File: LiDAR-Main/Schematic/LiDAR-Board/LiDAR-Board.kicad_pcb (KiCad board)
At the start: 2 copper layers, 8 parts, among them Q1 NPN, Q2 NPN, U1 Pico

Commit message: PCB Finished w/earths
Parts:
- added J1: Conn_01x04, HEVCS_Sensor_Footprints:Conn_01x04_MOLEX, F.Cu at (49.3, 20.3)
- moved R1 45.8 mm to (76.2, 66.0)
- moved Q2 44.1 mm to (82.2, 67.6)
- moved R2 43.7 mm to (76.2, 68.6)
- moved Q1 43.6 mm to (82.2, 61.9)
- moved U4 37.8 mm to (40.6, 48.3)
- moved U1 28.1 mm to (59.8, 52.1)
- moved U2 28.1 mm to (104.1, 33.0)
- moved U3 28.1 mm to (104.1, 48.3)
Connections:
- net +5V renamed 5V_MAIN_BOARD
- R1 pad 1: Net-(U1-GPIO21) -> Net-(U1-GPIO19)
- R2 pad 1: Net-(U1-GPIO20) -> Net-(U1-GPIO18)
- U1 pad 17: unconnected-(U1-GPIO13-Pad17) -> IMU_INT
- U1 pad 18: IMU_INT -> unconnected-(U1-GND-Pad18)
- U1 pad 19: INT_1 -> unconnected-(U1-GPIO14-Pad19)
- U1 pad 20: INT_2 -> unconnected-(U1-GPIO15-Pad20)
- U1 pad 21: unconnected-(U1-GPIO16-Pad21) -> INT_2
- U1 pad 22: unconnected-(U1-GPIO17-Pad22) -> INT_1
- U1 pad 23: unconnected-(U1-GND-Pad23) -> Earth
- U1 pad 24: unconnected-(U1-GPIO18-Pad24) -> Net-(U1-GPIO18)
- U1 pad 25: unconnected-(U1-GPIO19-Pad25) -> Net-(U1-GPIO19)
- U1 pad 26: Net-(U1-GPIO20) -> SDA
- U1 pad 27: Net-(U1-GPIO21) -> SCL
- U1 pad 3: unconnected-(U1-GND-Pad3) -> Earth
- U1 pad 6: SCL -> unconnected-(U1-GPIO4-Pad6)
- U1 pad 7: SDA -> unconnected-(U1-GPIO5-Pad7)
- U2 pad 5: (no net) -> Earth
- U3 pad 5: (no net) -> Earth
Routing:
- net SDA: track 0.00 -> 146.1 mm
- net INT_1: track 0.00 -> 105.8 mm
- net 3V3_BOARD_OUT: track 0.00 -> 74.4 mm
- net INT_2: track 0.00 -> 61.5 mm
- net 5V_MAIN_BOARD: track 0.00 -> 57.8 mm
- net Earth: track 0.00 -> 54.5 mm
- net Net-(Q1-C): track 0.00 -> 40.4 mm
- net Net-(Q2-C): track 0.00 -> 33.5 mm
- net SCL: track 0.00 -> 28.8 mm
- net IMU_INT: track 0.00 -> 21.0 mm
- net UART_0_RX: track 0.00 -> 15.0 mm
- net IMU_SDA: track 0.00 -> 10.3 mm
- net IMU_SCL: track 0.00 -> 10.3 mm
- net UART_0_TX: track 0.00 -> 7.66 mm
- net Net-(U1-GPIO19): track 0.00 -> 6.69 mm
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
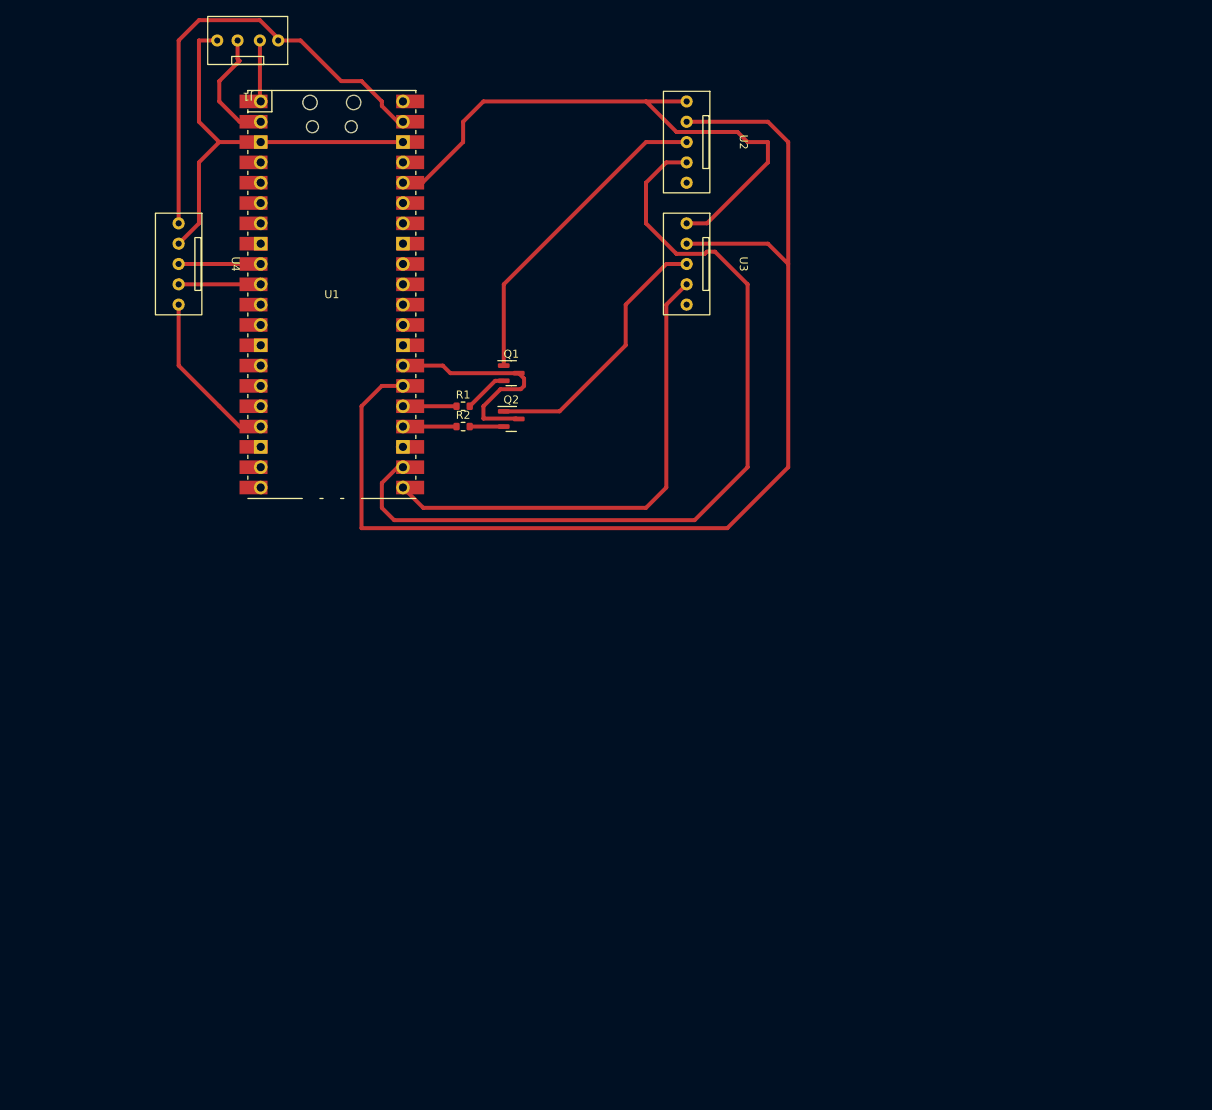
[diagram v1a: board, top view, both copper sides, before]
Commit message: Refactor PCB - can be reverted if wanted :)
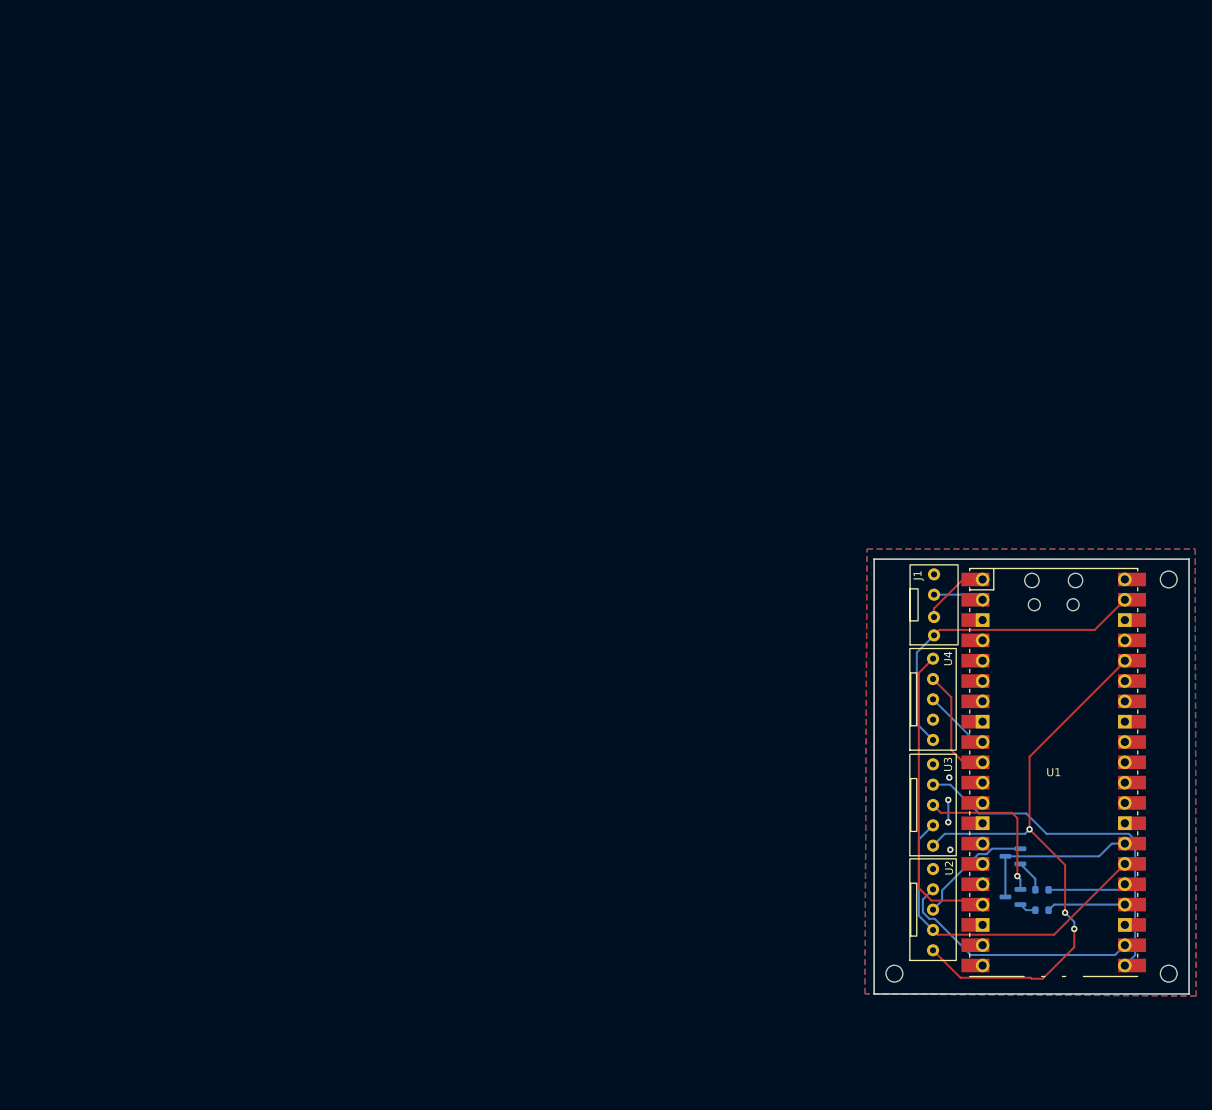
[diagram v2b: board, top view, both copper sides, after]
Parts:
- added REF**: MountingHole_2.1mm, MountingHole:MountingHole_2.1mm, F.Cu at (164.4, 137.0)
- added REF**: MountingHole_2.1mm, MountingHole:MountingHole_2.1mm, F.Cu at (130.1, 137.0)
- added REF**: MountingHole_2.1mm, MountingHole:MountingHole_2.1mm, F.Cu at (164.4, 87.7)
- Q1, Q2, R1, R2: moved to B.Cu
- moved J1 111.1 mm to (135.1, 90.9), turned to 90 degrees
- moved U4 108.9 mm to (134.9, 102.7), turned to 90 degrees
- moved U1 108.2 mm to (150.0, 111.8)
- moved U2 100.8 mm to (134.9, 129.0), turned to 90 degrees
- moved R2 94.3 mm to (148.6, 129.0), turned to 180 degrees
- moved R1 94.3 mm to (148.6, 126.5), turned to 180 degrees
- moved Q1 87.1 mm to (144.9, 122.3), turned to 180 degrees
- moved Q2 86.6 mm to (144.9, 127.4), turned to 180 degrees
- moved U3 74.3 mm to (134.9, 115.9), turned to 90 degrees
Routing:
- net SDA: track 146.1 -> 42.4 mm
- net INT_1: track 105.8 -> 31.4 mm
- net Earth: track 54.5 -> 2.79 mm, vias 0 -> 4
- net Net-(Q1-C): track 40.4 -> 14.8 mm
- net 5V_MAIN_BOARD: track 57.8 -> 40.5 mm
- net IMU_INT: track 21.0 -> 38.2 mm
- net INT_2: track 61.5 -> 44.4 mm
- net Net-(Q2-C): track 33.5 -> 20.3 mm, vias 0 -> 1
- net UART_0_RX: track 15.0 -> 6.33 mm
- net SCL: track 28.8 -> 20.7 mm
- net IMU_SDA: track 10.3 -> 14.4 mm
- net Net-(U1-GPIO18): track 6.69 -> 9.82 mm
- net Net-(U1-GPIO19): track 6.69 -> 9.82 mm
- net 3V3_BOARD_OUT: track 74.4 -> 76.7 mm, vias 0 -> 3
- net Net-(Q2-B): track 4.25 -> 2.16 mm
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- added copper zone on B.Cu, net Earth
- added copper zone on F.Cu, net Earth
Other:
- board outline added: 39.4 x 54.4 mm

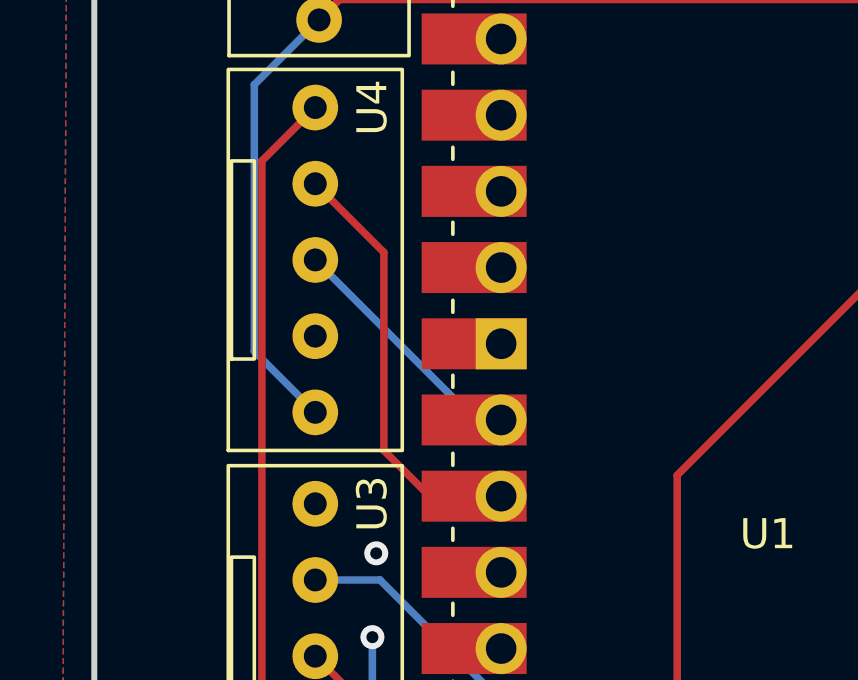
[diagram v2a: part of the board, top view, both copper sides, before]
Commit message: Fixed IMU I2C Pin allocation
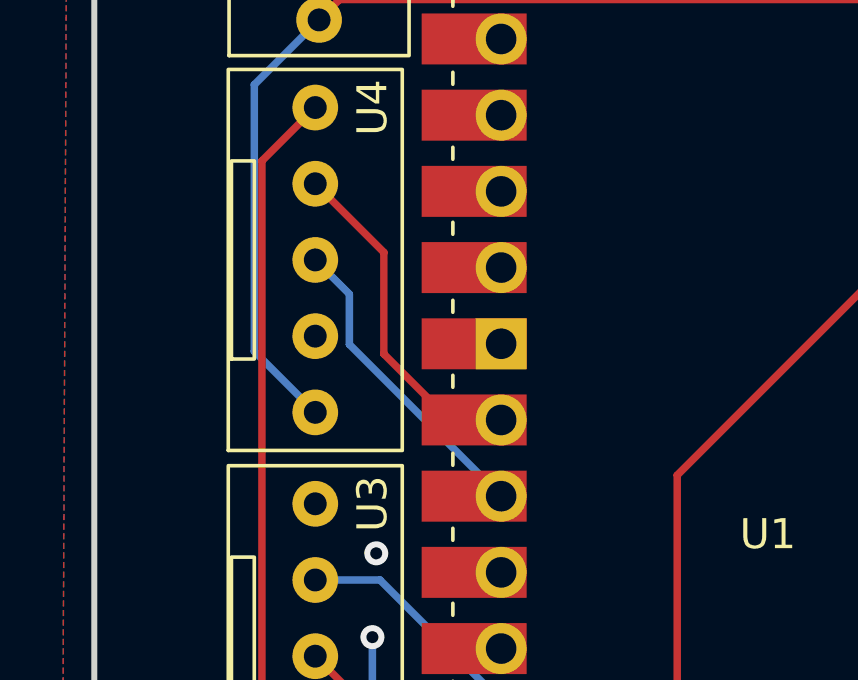
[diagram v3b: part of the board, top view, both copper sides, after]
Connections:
- U1 pad 10: IMU_SDA -> IMU_SCL
- U1 pad 9: IMU_SCL -> IMU_SDA
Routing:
- net IMU_SDA: track 14.4 -> 11.4 mm
- net IMU_SCL: track 8.41 -> 10.4 mm
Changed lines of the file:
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@@
       (net 11 "unconnected-(U1-GND-Pad8)") (pinfunction "GND") (pintype "power_in+no_connect"))
     (pad "9" thru_hole oval (at -8.89 -3.81) (size 1.7 1.7) (drill 1.02) (layers "*.Cu" "*.Mask")
-      (net 12 "IMU_SCL") (pinfunction "GPIO6") (pintype "bidirectional"))
+      (net 13 "IMU_SDA") (pinfunction "GPIO6") (pintype "bidirectional"))
     (pad "9" smd rect (at -8.89 -3.81) (size 3.5 1.7) (drill (offset -0.9 0)) (layers "F.Cu" "F.Mask")
-      (net 12 "IMU_SCL") (pinfunction "GPIO6") (pintype "bidirectional"))
+      (net 13 "IMU_SDA") (pinfunction "GPIO6") (pintype "bidirectional"))
     (pad "10" thru_hole oval (at -8.89 -1.27) (size 1.7 1.7) (drill 1.02) (layers "*.Cu" "*.Mask")
-      (net 13 "IMU_SDA") (pinfunction "GPIO7") (pintype "bidirectional"))
+      (net 12 "IMU_SCL") (pinfunction "GPIO7") (pintype "bidirectional"))
     (pad "10" smd rect (at -8.89 -1.27) (size 3.5 1.7) (drill (offset -0.9 0)) (layers "F.Cu" "F.Mask")
-      (net 13 "IMU_SDA") (pinfunction "GPIO7") (pintype "bidirectional"))
+      (net 12 "IMU_SCL") (pinfunction "GPIO7") (pintype "bidirectional"))
     (pad "11" thru_hole oval (at -8.89 1.27) (size 1.7 1.7) (drill 1.02) (layers "*.Cu" "*.Mask")
-      (net 14 "unconnected-(U1-GPIO8-Pad11)") (pinfunction "GPIO8") (pintype "bidirectional+no_connect"))
+      (net 14 "unconnected-(U1-GPIO8-Pad11)") (pinfunction "GPIO8") (pintype "bidirectional"))
     (pad "11" smd rect (at -8.89 1.27) (size 3.5 1.7) (drill (offset -0.9 0)) (layers "F.Cu" "F.Mask")
-      (net 14 "unconnected-(U1-GPIO8-Pad11)") (pinfunction "GPIO8") (pintype "bidirectional+no_connect"))
+      (net 14 "unconnected-(U1-GPIO8-Pad11)") (pinfunction "GPIO8") (pintype "bidirectional"))
     (pad "12" thru_hole oval (at -8.89 3.81) (size 1.7 1.7) (drill 1.02) (layers "*.Cu" "*.Mask")
       (net 15 "unconnected-(U1-GPIO9-Pad12)") (pinfunction "GPIO9") (pintype "bidirectional+no_connect"))
@@
   (segment (start 134.94 131.506) (end 133.17 129.736) (width 0.25) (layer "B.Cu") (net 10))
   (segment (start 133.17 129.736) (end 133.17 120.195) (width 0.25) (layer "B.Cu") (net 10))
-  (segment (start 134.94 102.677) (end 140.274 108.011) (width 0.25) (layer "B.Cu") (net 12))
-  (segment (start 140.274 108.011) (end 141.136 108.011) (width 0.25) (layer "B.Cu") (net 12))
-  (segment (start 138.75 110.551) (end 141.136 110.551) (width 0.25) (layer "F.Cu") (net 13))
-  (segment (start 137.226 109.027) (end 138.75 110.551) (width 0.25) (layer "F.Cu") (net 13))
-  (segment (start 134.94 100.137) (end 137.226 102.423) (width 0.25) (layer "F.Cu") (net 13))
-  (segment (start 137.226 102.423) (end 137.226 109.027) (width 0.25) (layer "F.Cu") (net 13))
+  (segment (start 136.077 105.492) (end 141.136 110.551) (width 0.25) (layer "B.Cu") (net 12))
+  (segment (start 134.94 102.677) (end 136.077 103.814) (width 0.25) (layer "B.Cu") (net 12))
+  (segment (start 136.077 103.814) (end 136.077 105.492) (width 0.25) (layer "B.Cu") (net 12))
+  (segment (start 137.226 102.423) (end 134.94 100.137) (width 0.25) (layer "F.Cu") (net 13))
+  (segment (start 137.226 105.811) (end 137.226 102.423) (width 0.25) (layer "F.Cu") (net 13))
+  (segment (start 141.136 108.011) (end 139.426 108.011) (width 0.25) (layer "F.Cu") (net 13))
+  (segment (start 139.426 108.011) (end 137.226 105.811) (width 0.25) (layer "F.Cu") (net 13))
   (segment (start 133.162 99.375) (end 133.162 126.255961) (width 0.25) (layer "F.Cu") (net 20))
   (segment (start 140.634 127.829) (end 141.136 128.331) (width 0.25) (layer "F.Cu") (net 20))

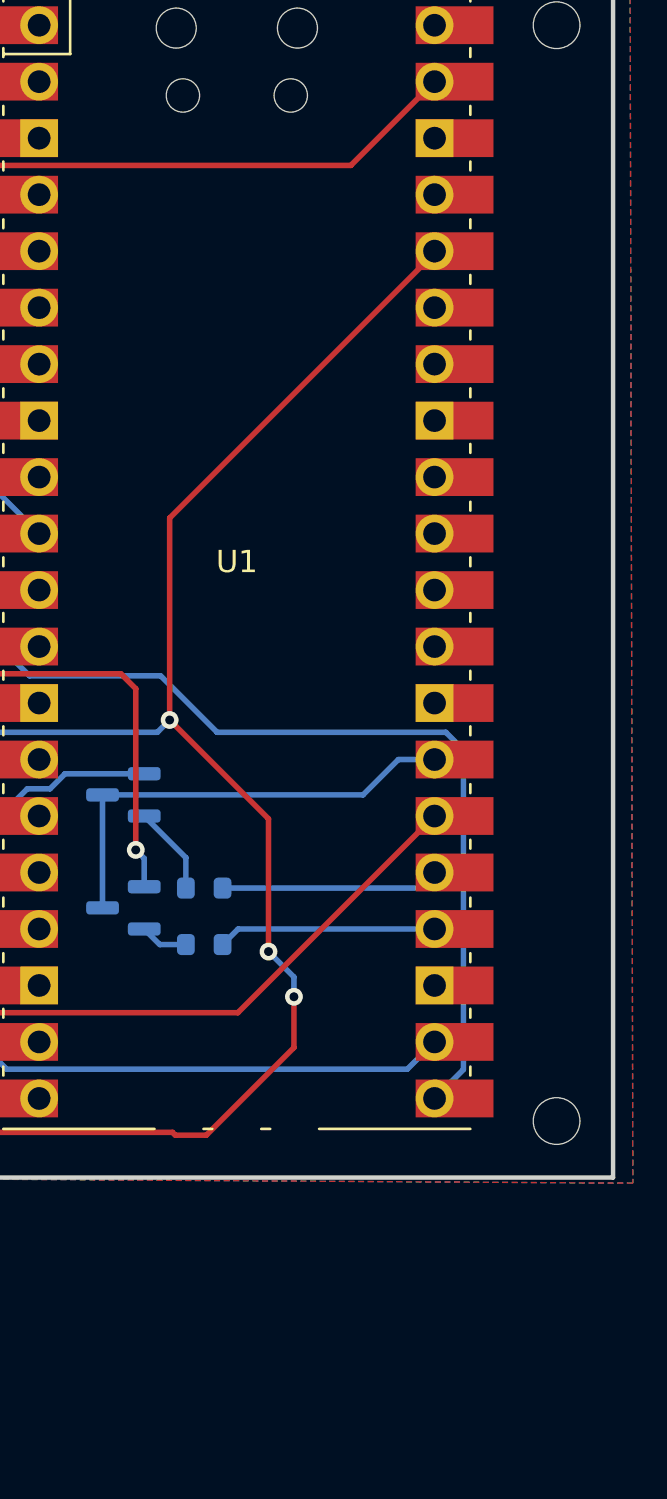
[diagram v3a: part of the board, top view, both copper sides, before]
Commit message: PCB Silkscreen changes
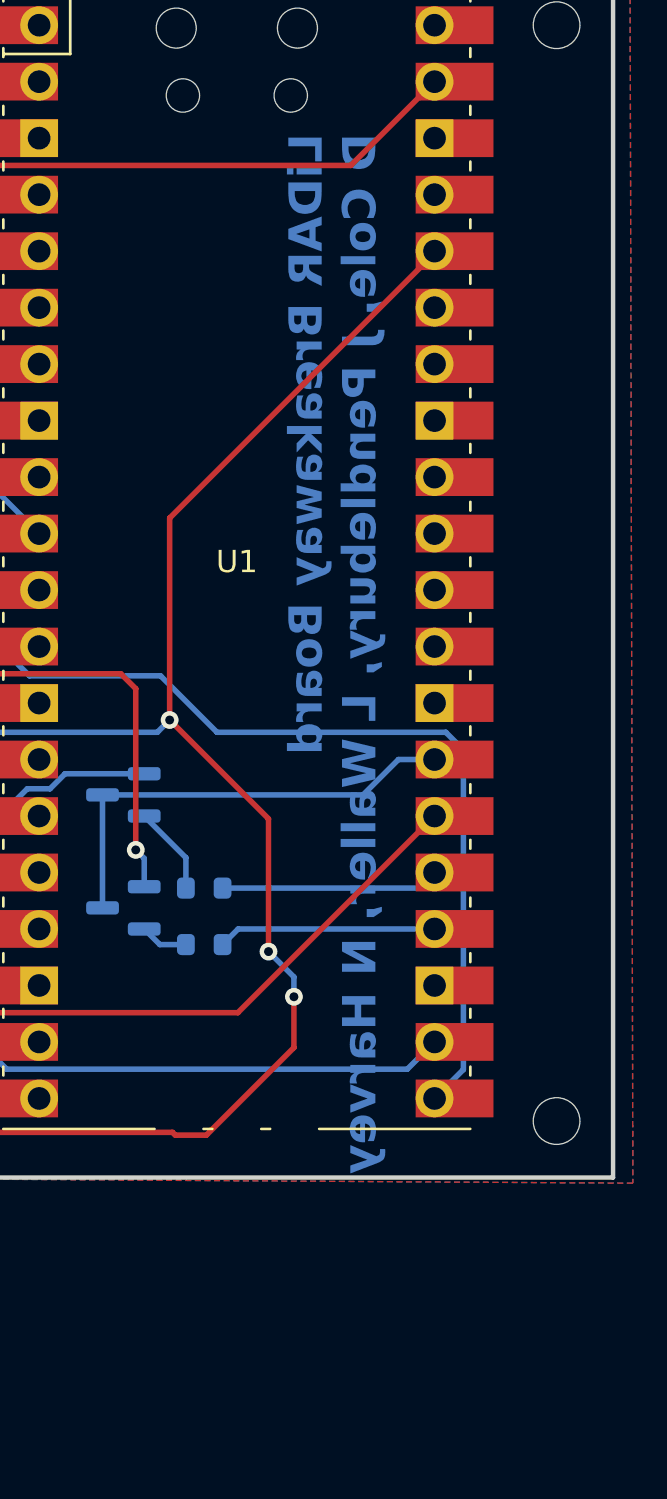
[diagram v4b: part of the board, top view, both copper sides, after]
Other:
- board text added: "LiDAR Breakaway Board D Cole, J Pendlebury, L Waller, N Harvey"
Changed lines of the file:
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@@
   (gr_rect (start 127.574 85.151) (end 166.944 139.507)
     (stroke (width 0.2) (type default)) (fill none) (layer "Edge.Cuts"))
+  (gr_text "LiDAR Breakaway Board\nD Cole, J Pendlebury, L Waller, N Harvey" (at 156.4386 92.5576 90) (layer "B.Cu")
+    (effects (font (size 1.5 1.5) (thickness 0.3) bold) (justify left bottom mirror))
+  )
   (segment (start 145.862 121.351) (end 142.301 121.351) (width 0.25) (layer "B.Cu") (net 1))
   (segment (start 136.077 127.829) (end 134.94 128.966) (width 0.25) (layer "B.Cu") (net 1))
